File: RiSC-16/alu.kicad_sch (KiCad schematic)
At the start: 7 parts, among them U1 74LS257, U11 74LS181, U4 74LS257

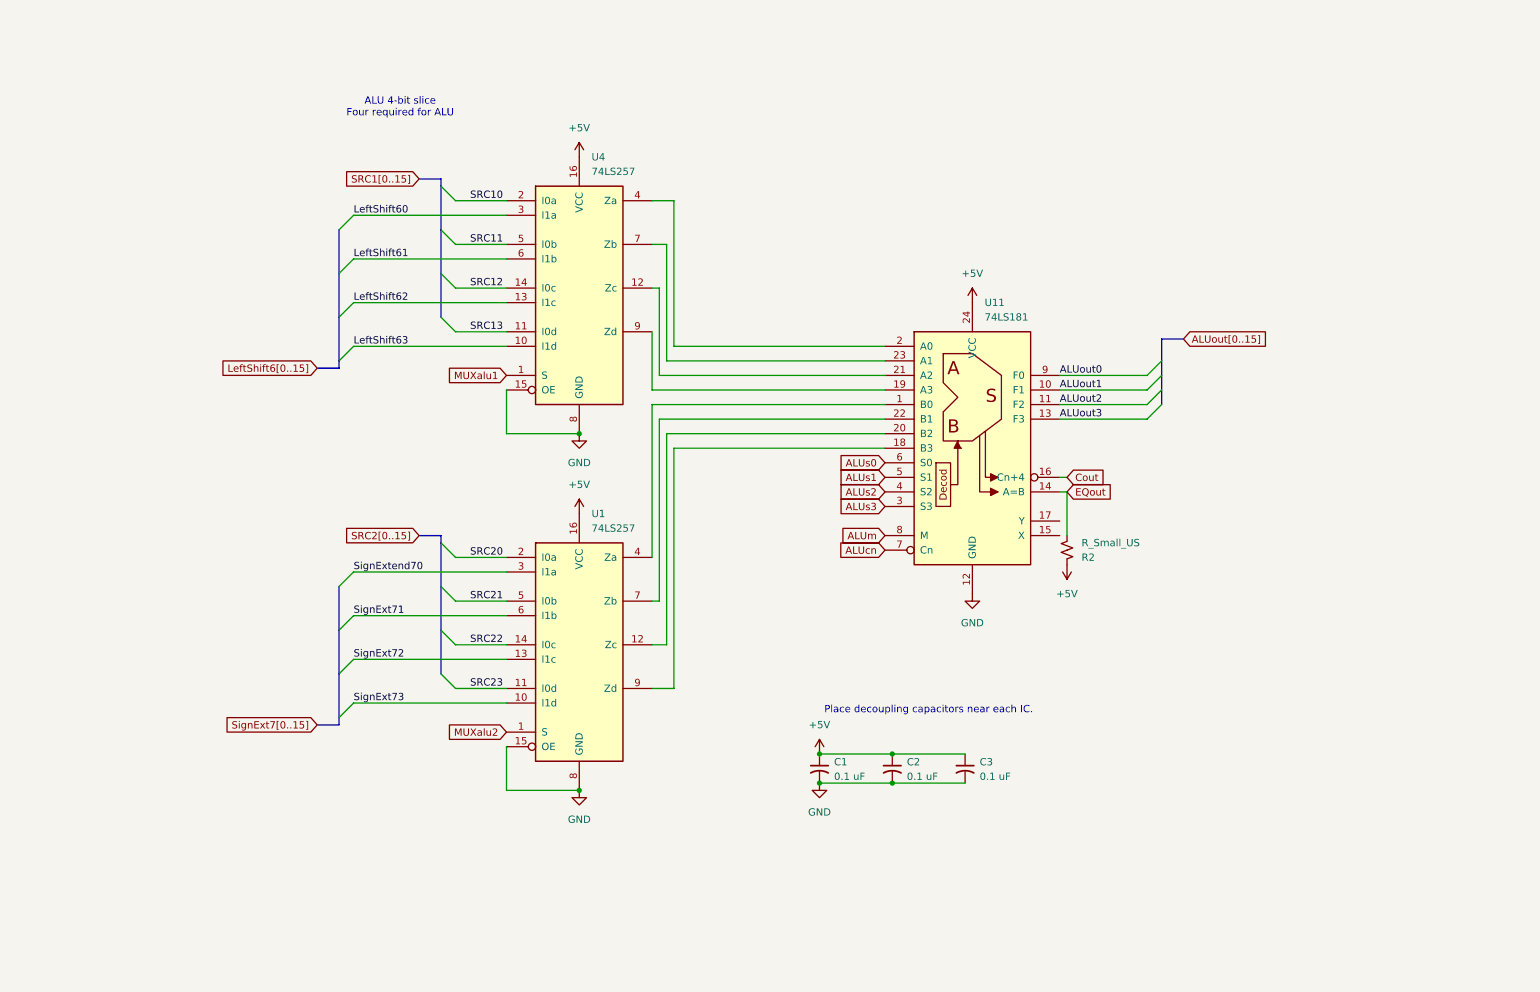
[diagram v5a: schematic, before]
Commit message: Added a custom symbol for the AM29705. Reworked to use it in two different approaches.
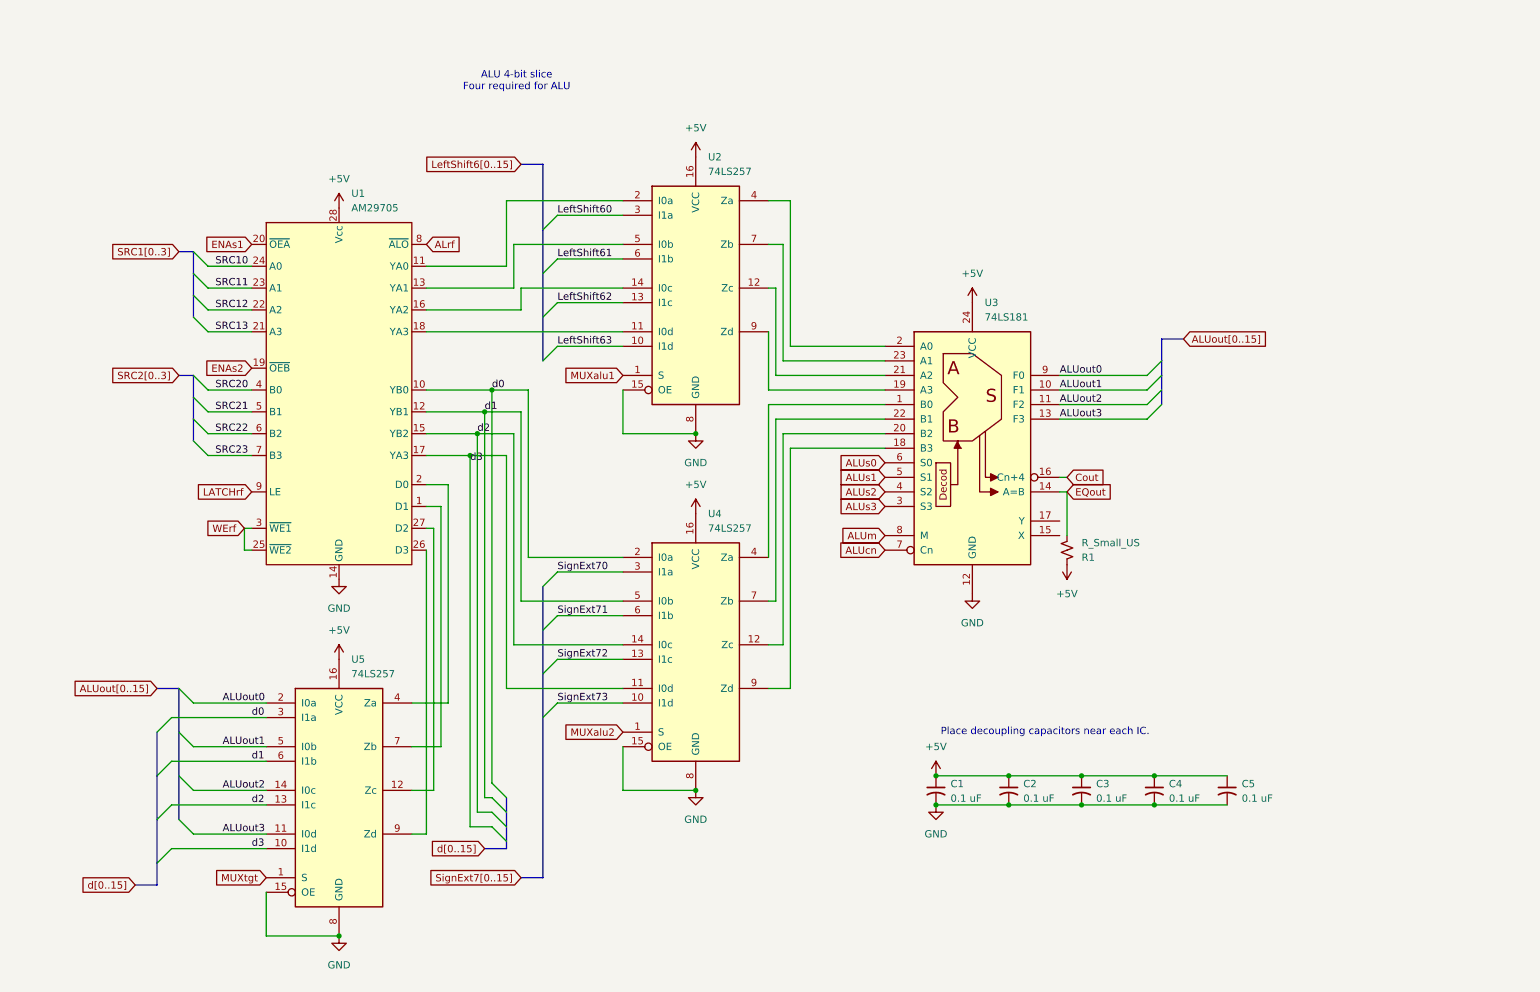
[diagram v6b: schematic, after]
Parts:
- added C4, C5: 0.1 uF, symbol Device:C_Small_US
- added U1: AM29705, symbol AMD Bit Slice:AM29705_Register_File
- added U5: 74LS257, symbol 74xx:74LS257
- renumbered R2 to R1, U4 to U2, U11 to U3, U1 to U4
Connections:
- net +5V: now also C4.1, C5.1, U1.28 (Vcc), U5.16 (VCC)
- net ALUout0: now also U5.2 (I0a)
- net ALUout1: now also U5.5 (I0b)
- net ALUout2: now also U5.14 (I0c)
- net ALUout3: now also U5.11 (I0d)
- net GND: now also C4.2, C5.2, U1.14 (GND), U5.15 (OE), U5.8 (GND)
- net SRC10: now also U1.24 (A0); no longer U2.2 (I0a)
- net SRC11: now also U1.23 (A1); no longer U2.5 (I0b)
- net SRC12: now also U1.22 (A2); no longer U2.14 (I0c)
- net SRC13: now also U1.21 (A3); no longer U2.11 (I0d)
- net SRC20: now also U1.4 (B0); no longer U4.2 (I0a)
- net SRC21: now also U1.5 (B1); no longer U4.5 (I0b)
- net SRC22: now also U1.6 (B2); no longer U4.14 (I0c)
- net SRC23: now also U1.7 (B3); no longer U4.11 (I0d)
- net SignExtend70 renamed SignExt70
- new net: U1.27 (D2), U5.12 (Zc)
- new net: U1.2 (D0), U5.4 (Za)
- new net: U1.1 (D1), U5.7 (Zb)
- new net: U1.26 (D3), U5.9 (Zd)
- new net: U1.18 (YA3), U2.11 (I0d)
- new net: U1.16 (YA2), U2.14 (I0c)
- new net: U1.11 (YA0), U2.2 (I0a)
- new net: U1.13 (YA1), U2.5 (I0b)
- new net ALrf: U1.8 (~{ALO})
- new net ENAs1: U1.20 (~{OEA})
- new net ENAs2: U1.19 (~{OEB})
- new net LATCHrf: U1.9 (LE)
- new net MUXtgt: U5.1 (S)
- new net WErf: U1.25 (~{WE2}), U1.3 (~{WE1})
- new net d0: U1.10 (YB0), U4.2 (I0a), U5.3 (I1a)
- new net d1: U1.12 (YB1), U4.5 (I0b), U5.6 (I1b)
- new net d2: U1.15 (YB2), U4.14 (I0c), U5.13 (I1c)
- new net d3: U1.17 (YA3), U4.11 (I0d), U5.10 (I1d)
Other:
- moved on the sheet: C1, C2, C3, U2, U4

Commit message: Moved and renamed pages.
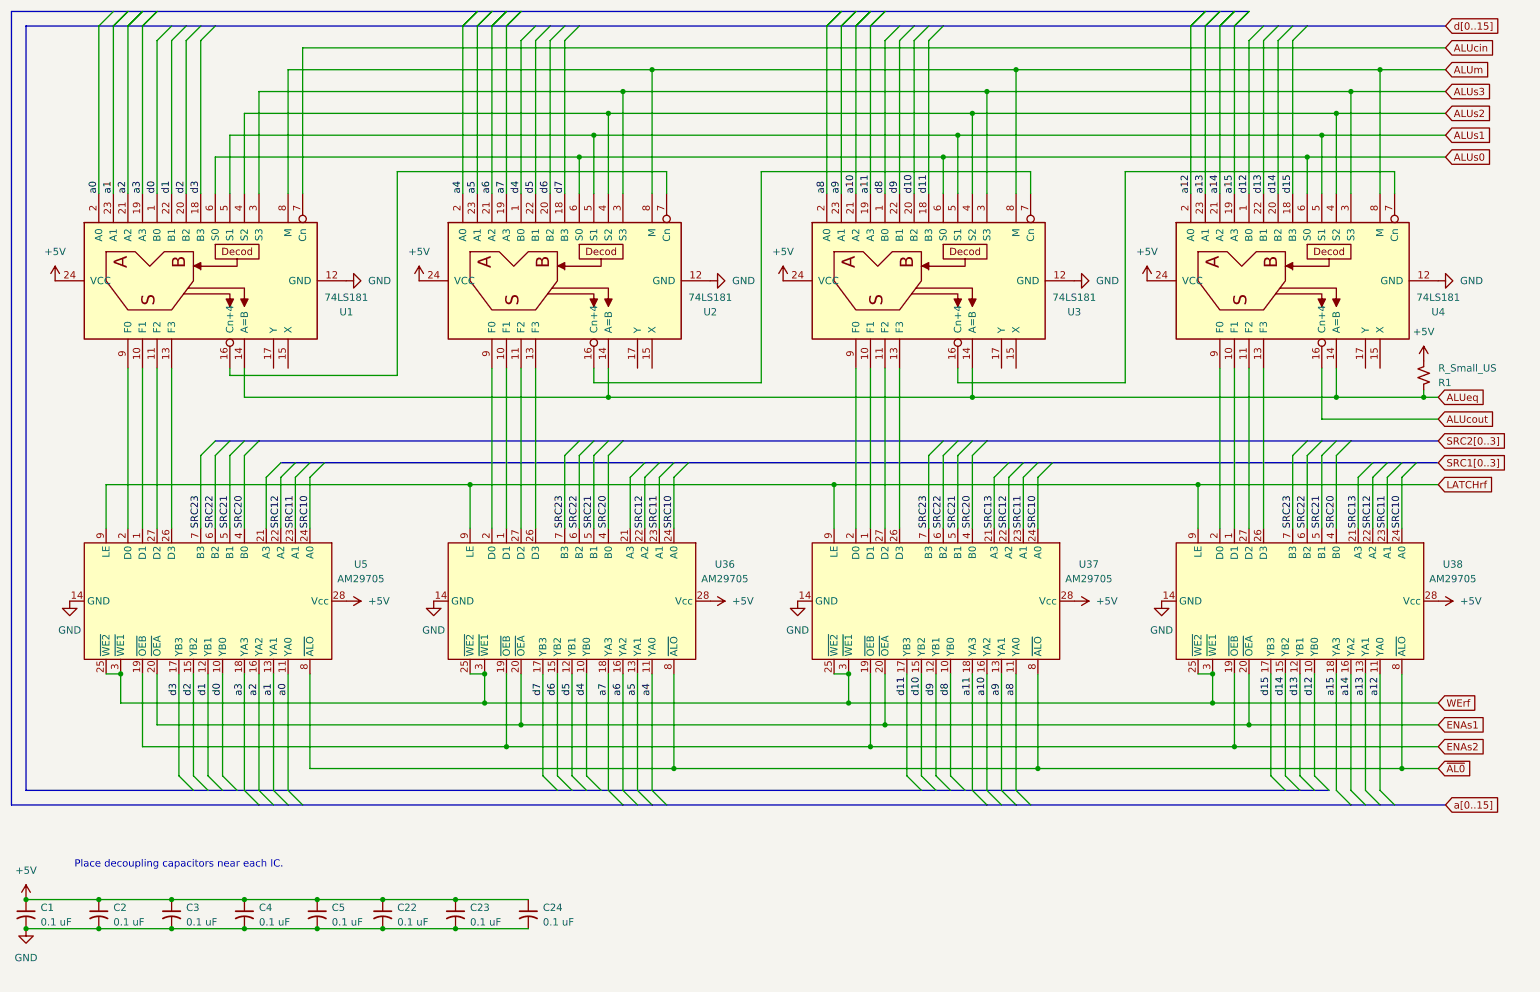
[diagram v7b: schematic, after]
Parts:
- removed U1: AM29705, symbol AMD Bit Slice:AM29705_Register_File
- removed U2, U4, U5: 74LS257, symbol 74xx:74LS257
- added C22, C23, C24: 0.1 uF, symbol Device:C_Small_US
- added U1, U2, U4: 74LS181, symbol 74xx:74LS181
- added U36, U37, U38, U5: AM29705, symbol AMD Bit Slice:AM29705_Register_File
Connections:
- net +5V: now also R1.2, C22.1, C23.1, C24.1, U1.24 (VCC), U2.24 (VCC), U36.28 (Vcc), U37.28 (Vcc), U38.28 (Vcc), U4.24 (VCC), U5.28 (Vcc); no longer R1.1
- net ALUm: now also U1.8 (M), U2.8 (M), U4.8 (M)
- net ALUs0: now also U1.6 (S0), U2.6 (S0), U4.6 (S0)
- net ALUs1: now also U1.5 (S1), U2.5 (S1), U4.5 (S1)
- net ALUs2: now also U1.4 (S2), U2.4 (S2), U4.4 (S2)
- net ALUs3: now also U1.3 (S3), U2.3 (S3), U4.3 (S3)
- net ENAs1: now also U36.20 (~{OEA}), U37.20 (~{OEA}), U38.20 (~{OEA}), U5.20 (~{OEA})
- net ENAs2: now also U36.19 (~{OEB}), U37.19 (~{OEB}), U38.19 (~{OEB}), U5.19 (~{OEB})
- net GND: now also C22.2, C23.2, C24.2, U1.12 (GND), U2.12 (GND), U36.14 (GND), U37.14 (GND), U38.14 (GND), U4.12 (GND), U5.14 (GND)
- net LATCHrf: now also U36.9 (LE), U37.9 (LE), U38.9 (LE), U5.9 (LE)
- net SRC10: now also U36.24 (A0), U37.24 (A0), U38.24 (A0), U5.24 (A0)
- net SRC11: now also U36.23 (A1), U37.23 (A1), U38.23 (A1), U5.23 (A1)
- net SRC12: now also U36.22 (A2), U37.22 (A2), U38.22 (A2), U5.22 (A2)
- net SRC13: now also U37.21 (A3), U38.21 (A3)
- net SRC20: now also U36.4 (B0), U37.4 (B0), U38.4 (B0), U5.4 (B0)
- net SRC21: now also U36.5 (B1), U37.5 (B1), U38.5 (B1), U5.5 (B1)
- net SRC22: now also U36.6 (B2), U37.6 (B2), U38.6 (B2), U5.6 (B2)
- net SRC23: now also U36.7 (B3), U37.7 (B3), U38.7 (B3), U5.7 (B3)
- net WErf: now also U36.25 (~{WE2}), U36.3 (~{WE1}), U37.25 (~{WE2}), U37.3 (~{WE1}), U38.25 (~{WE2}), U38.3 (~{WE1}), U5.25 (~{WE2}), U5.3 (~{WE1})
- net d0: now also U1.1 (B0), U5.10 (YB0)
- net d1: now also U1.22 (B1), U5.12 (YB1)
- net d2: now also U1.20 (B2), U5.15 (YB2)
- net d3: now also U1.18 (B3), U5.17 (YB3)
- net d10: now reaches U3.20 (B2)
- net d10: now also U37.15 (YB2)
- net d8: now reaches U3.1 (B0)
- net d8: now also U37.10 (YB0)
- net d9: now reaches U3.22 (B1)
- net d9: now also U37.12 (YB1)
- net d11: now reaches U3.18 (B3)
- net d11: now also U37.17 (YB3)
- net a11: now reaches U3.19 (A3)
- net a11: now also U37.18 (YA3)
- net a8: now reaches U3.2 (A0)
- net a8: now also U37.11 (YA0)
- net a10: now reaches U3.21 (A2)
- net a10: now also U37.16 (YA2)
- net a9: now reaches U3.23 (A1)
- net a9: now also U37.13 (YA1)
- net ALUcn: no longer names the net of U3.7 (Cn)
- net ALUcn: now also U2.16 (Cn+4)
- net ALUout0: no longer names the net of U3.9 (F0)
- net ALUout0: now also U37.2 (D0)
- net ALUout1: no longer names the net of U3.10 (F1)
- net ALUout1: now also U37.1 (D1)
- net ALUout2: no longer names the net of U3.11 (F2)
- net ALUout2: now also U37.27 (D2)
- net ALUout3: no longer names the net of U3.13 (F3)
- net ALUout3: now also U37.26 (D3)
- net Cout: no longer names the net of U3.16 (Cn+4)
- net Cout: now also U4.7 (Cn)
- net EQout renamed ALUeq
- net ALUeq: now also R1.1, U1.14 (A=B), U2.14 (A=B), U4.14 (A=B); no longer R1.2
- new net: U2.10 (F1), U36.1 (D1)
- new net: U2.9 (F0), U36.2 (D0)
- new net: U2.13 (F3), U36.26 (D3)
- new net: U2.11 (F2), U36.27 (D2)
- new net: U1.10 (F1), U5.1 (D1)
- new net: U1.9 (F0), U5.2 (D0)
- new net: U1.13 (F3), U5.26 (D3)
- new net: U1.11 (F2), U5.27 (D2)
- new net: U38.1 (D1), U4.10 (F1)
- new net: U38.27 (D2), U4.11 (F2)
- new net: U38.26 (D3), U4.13 (F3)
- new net: U38.2 (D0), U4.9 (F0)
- new net: U1.16 (Cn+4), U2.7 (Cn)
- new net ALUcin: U1.7 (Cn)
- new net ALUcout: U4.16 (Cn+4)
- new net a0: U1.2 (A0), U5.11 (YA0)
- new net a1: U1.23 (A1), U5.13 (YA1)
- new net a12: U38.11 (YA0), U4.2 (A0)
- new net a13: U38.13 (YA1), U4.23 (A1)
- new net a14: U38.16 (YA2), U4.21 (A2)
- new net a15: U38.18 (YA3), U4.19 (A3)
- new net a2: U1.21 (A2), U5.16 (YA2)
- new net a3: U1.19 (A3), U5.18 (YA3)
- new net a4: U2.2 (A0), U36.11 (YA0)
- new net a5: U2.23 (A1), U36.13 (YA1)
- new net a6: U2.21 (A2), U36.16 (YA2)
- new net a7: U2.19 (A3), U36.18 (YA3)
- new net d12: U38.10 (YB0), U4.1 (B0)
- new net d13: U38.12 (YB1), U4.22 (B1)
- new net d14: U38.15 (YB2), U4.20 (B2)
- new net d15: U38.17 (YB3), U4.18 (B3)
- new net d4: U2.1 (B0), U36.10 (YB0)
- new net d5: U2.22 (B1), U36.12 (YB1)
- new net d6: U2.20 (B2), U36.15 (YB2)
- new net d7: U2.18 (B3), U36.17 (YB3)
- new net ~{AL0}: U36.8 (~{ALO}), U37.8 (~{ALO}), U38.8 (~{ALO}), U5.8 (~{ALO})
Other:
- note removed: "ALU 4-bit slice Four required for ALU"

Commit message: Annotated the schematic to align part numbers. EPROM and RAM board was added last revision. Reworked the src1 latching to assert 0xf to select the PC.
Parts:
- renumbered C22 to C6, C23 to C7, C24 to C8, U36 to U6, U37 to U7, U38 to U8
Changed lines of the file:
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@@
 		(dnp no)
 		(fields_autoplaced yes)
-		(property "Reference" "U36"
+		(property "Reference" "U6"
 			(at 142.24 115.4998 90)
 			(effects
@@
 			(project "RiSC-16"
 				(path "/09ce4153-429f-4803-b069-3af485a81dd6/13fbf43c-26a0-4ef0-bac8-c4e84e3a9419"
-					(reference "U36")
+					(reference "U6")
 					(unit 1)
 				)
@@
 		(dnp no)
 		(fields_autoplaced yes)
-		(property "Reference" "#PWR074"
+		(property "Reference" "#PWR017"
 			(at 262.89 121.92 0)
 			(effects
@@
 			(project "RiSC-16"
 				(path "/09ce4153-429f-4803-b069-3af485a81dd6/13fbf43c-26a0-4ef0-bac8-c4e84e3a9419"
-					(reference "#PWR074")
+					(reference "#PWR017")
 					(unit 1)
 				)
@@
 		(dnp no)
 		(fields_autoplaced yes)
-		(property "Reference" "C23"
+		(property "Reference" "C7"
 			(at 97.79 175.3869 0)
 			(effects
@@
 			(project "RiSC-16"
 				(path "/09ce4153-429f-4803-b069-3af485a81dd6/13fbf43c-26a0-4ef0-bac8-c4e84e3a9419"
-					(reference "C23")
+					(reference "C7")
 					(unit 1)
 				)
@@
 		(dnp no)
 		(fields_autoplaced yes)
-		(property "Reference" "U37"
+		(property "Reference" "U7"
 			(at 205.74 115.4998 90)
 			(effects
@@
 			(project "RiSC-16"
 				(path "/09ce4153-429f-4803-b069-3af485a81dd6/13fbf43c-26a0-4ef0-bac8-c4e84e3a9419"
-					(reference "U37")
+					(reference "U7")
 					(unit 1)
 				)
@@
 		(dnp no)
 		(fields_autoplaced yes)
-		(property "Reference" "#PWR073"
+		(property "Reference" "#PWR016"
 			(at 218.44 128.27 0)
 			(effects
@@
 			(project "RiSC-16"
 				(path "/09ce4153-429f-4803-b069-3af485a81dd6/13fbf43c-26a0-4ef0-bac8-c4e84e3a9419"
-					(reference "#PWR073")
+					(reference "#PWR016")
 					(unit 1)
 				)
@@
 		(dnp no)
 		(fields_autoplaced yes)
-		(property "Reference" "#PWR076"
+		(property "Reference" "#PWR019"
 			(at 20.32 185.42 0)
 			(effects
@@
 			(project "RiSC-16"
 				(path "/09ce4153-429f-4803-b069-3af485a81dd6/13fbf43c-26a0-4ef0-bac8-c4e84e3a9419"
-					(reference "#PWR076")
+					(reference "#PWR019")
 					(unit 1)
 				)
@@
 		(dnp no)
 		(fields_autoplaced yes)
-		(property "Reference" "#PWR071"
+		(property "Reference" "#PWR014"
 			(at 154.94 128.27 0)
 			(effects
@@
 			(project "RiSC-16"
 				(path "/09ce4153-429f-4803-b069-3af485a81dd6/13fbf43c-26a0-4ef0-bac8-c4e84e3a9419"
-					(reference "#PWR071")
+					(reference "#PWR014")
 					(unit 1)
 				)
@@
 		(dnp no)
 		(fields_autoplaced yes)
-		(property "Reference" "C22"
+		(property "Reference" "C6"
 			(at 85.09 175.3869 0)
 			(effects
@@
 			(project "RiSC-16"
 				(path "/09ce4153-429f-4803-b069-3af485a81dd6/13fbf43c-26a0-4ef0-bac8-c4e84e3a9419"
-					(reference "C22")
+					(reference "C6")
 					(unit 1)
 				)
@@
 		(dnp no)
 		(fields_autoplaced yes)
-		(property "Reference" "#PWR072"
+		(property "Reference" "#PWR015"
 			(at 199.39 121.92 0)
 			(effects
@@
 			(project "RiSC-16"
 				(path "/09ce4153-429f-4803-b069-3af485a81dd6/13fbf43c-26a0-4ef0-bac8-c4e84e3a9419"
-					(reference "#PWR072")
+					(reference "#PWR015")
 					(unit 1)
 				)
@@
 		(dnp no)
 		(fields_autoplaced yes)
-		(property "Reference" "U38"
+		(property "Reference" "U8"
 			(at 269.24 115.4998 90)
 			(effects
@@
 			(project "RiSC-16"
 				(path "/09ce4153-429f-4803-b069-3af485a81dd6/13fbf43c-26a0-4ef0-bac8-c4e84e3a9419"
-					(reference "U38")
+					(reference "U8")
 					(unit 1)
 				)
@@
 		(dnp no)
 		(fields_autoplaced yes)
-		(property "Reference" "C24"
+		(property "Reference" "C8"
 			(at 110.49 175.3869 0)
 			(effects
@@
 			(project "RiSC-16"
 				(path "/09ce4153-429f-4803-b069-3af485a81dd6/13fbf43c-26a0-4ef0-bac8-c4e84e3a9419"
-					(reference "C24")
+					(reference "C8")
 					(unit 1)
 				)
@@
 		(dnp no)
 		(fields_autoplaced yes)
-		(property "Reference" "#PWR075"
+		(property "Reference" "#PWR018"
 			(at 20.32 177.8 0)
 			(effects
@@
 			(project "RiSC-16"
 				(path "/09ce4153-429f-4803-b069-3af485a81dd6/13fbf43c-26a0-4ef0-bac8-c4e84e3a9419"
-					(reference "#PWR075")
-					(unit 1)
-				)
+					(reference "#PWR018")
+					(unit 1)
+				)
